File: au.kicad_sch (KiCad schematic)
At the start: 14 parts, among them Q1 SUM110P06-08L, Q2 2N7002, Q3 2N7002

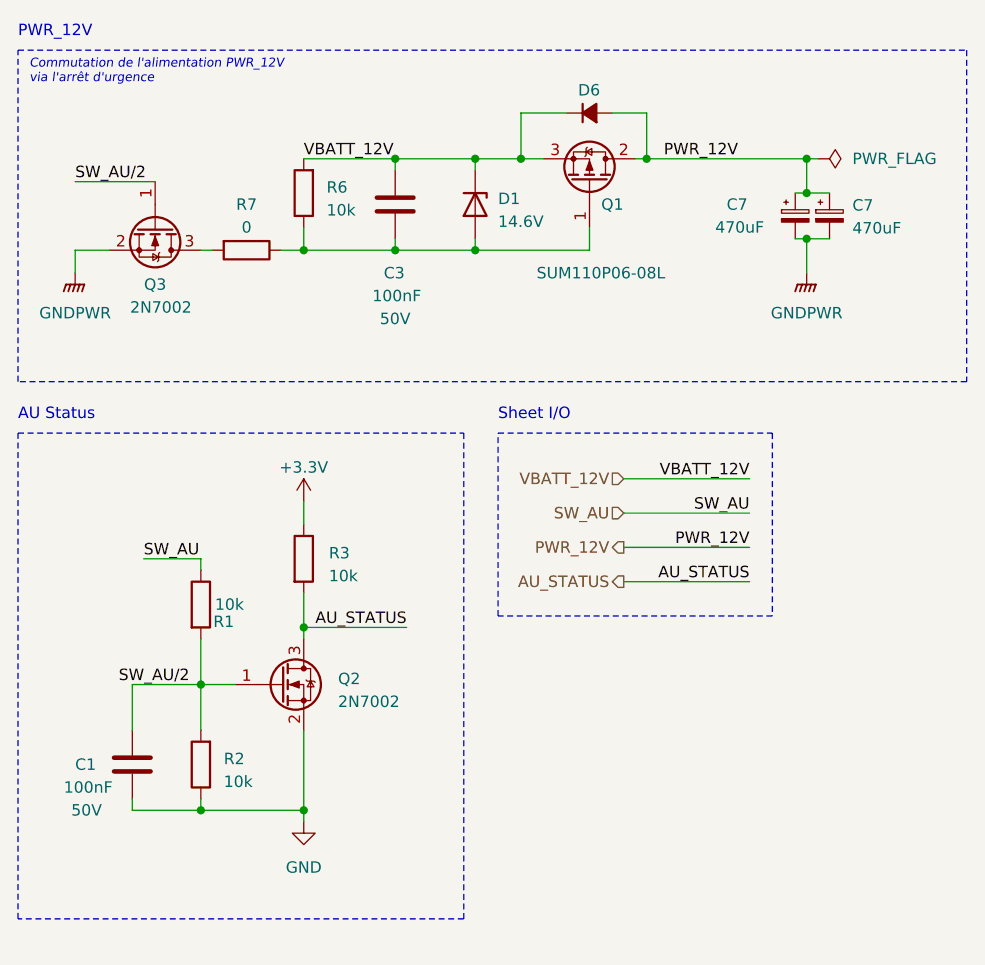
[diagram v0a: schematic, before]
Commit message: Correct CAN interface, add some filtering on sensors + add LCD board power connector
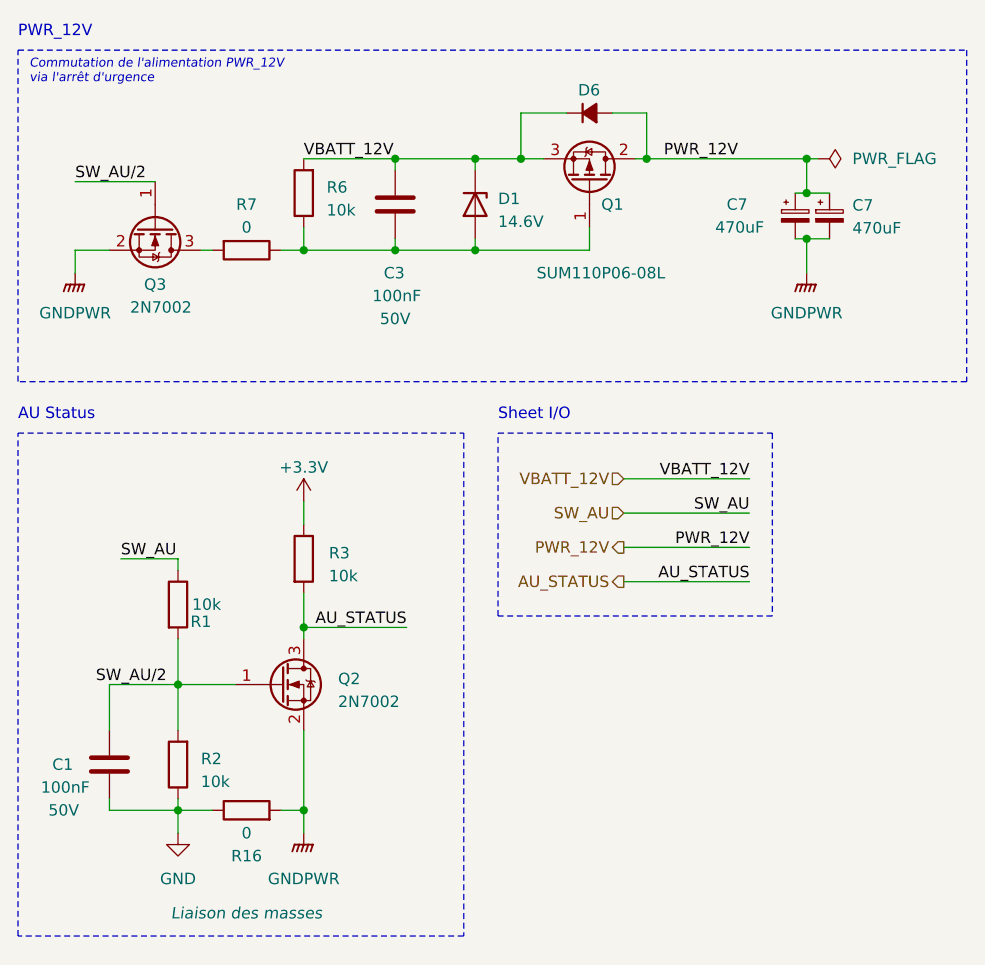
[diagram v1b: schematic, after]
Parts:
- added R16: 0, Resistor_SMD:R_0805_2012Metric, symbol Device:R
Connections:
- net GND: now also R16.1; no longer Q2.2 (S)
- net GNDPWR: now also Q2.2 (S), R16.2
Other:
- moved on the sheet: C1, R1, R2
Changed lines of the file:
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@@
   (junction (at 102.87 29.21) (diameter 0) (color 0 0 0 0)
   )
-  (junction (at 35.56 101.6) (diameter 0) (color 0 0 0 0)
+  (junction (at 33.02 101.6) (diameter 0) (color 0 0 0 0)
   )
-  (junction (at 35.56 87.63) (diameter 0) (color 0 0 0 0)
+  (junction (at 33.02 87.63) (diameter 0) (color 0 0 0 0)
   )
   (junction (at 102.87 33.02) (diameter 0) (color 0 0 0 0)
@@
     (stroke (width 0) (type default))
   )
-  (wire (pts (xy 35.56 82.55) (xy 35.56 87.63))
+  (wire (pts (xy 33.02 82.55) (xy 33.02 87.63))
     (stroke (width 0) (type default))
   )
@@
     (stroke (width 0) (type default))
   )
-  (wire (pts (xy 27.94 101.6) (xy 35.56 101.6))
+  (wire (pts (xy 25.4 101.6) (xy 33.02 101.6))
     (stroke (width 0) (type default))
   )
@@
     (stroke (width 0) (type default))
   )
-  (wire (pts (xy 35.56 87.63) (xy 39.37 87.63))
+  (wire (pts (xy 81.28 24.13) (xy 85.09 24.13))
     (stroke (width 0) (type default))
   )
-  (wire (pts (xy 81.28 24.13) (xy 85.09 24.13))
+  (wire (pts (xy 25.4 87.63) (xy 25.4 92.71))
     (stroke (width 0) (type default))
   )
-  (wire (pts (xy 27.94 87.63) (xy 27.94 92.71))
+  (wire (pts (xy 46.99 101.6) (xy 46.99 104.14))
     (stroke (width 0) (type default))
   )
-  (wire (pts (xy 46.99 101.6) (xy 46.99 102.87))
+  (wire (pts (xy 46.99 92.71) (xy 46.99 101.6))
     (stroke (width 0) (type default))
   )
@@
     (stroke (width 0) (type default))
   )
+  (wire (pts (xy 33.02 101.6) (xy 36.83 101.6))
+    (stroke (width 0) (type default))
+  )
   (wire (pts (xy 101.6 38.1) (xy 102.87 38.1))
     (stroke (width 0) (type default))
   )
+  (wire (pts (xy 33.02 101.6) (xy 33.02 104.14))
+    (stroke (width 0) (type default))
+  )
   (wire (pts (xy 66.04 39.37) (xy 57.15 39.37))
     (stroke (width 0) (type default))
@@
     (stroke (width 0) (type default))
   )
-  (wire (pts (xy 35.56 100.33) (xy 35.56 101.6))
+  (wire (pts (xy 33.02 100.33) (xy 33.02 101.6))
     (stroke (width 0) (type default))
   )
-  (wire (pts (xy 35.56 87.63) (xy 35.56 92.71))
+  (wire (pts (xy 33.02 87.63) (xy 33.02 92.71))
     (stroke (width 0) (type default))
   )
-  (wire (pts (xy 102.87 29.21) (xy 102.87 33.02))
+  (wire (pts (xy 33.02 87.63) (xy 39.37 87.63))
     (stroke (width 0) (type default))
   )
-  (wire (pts (xy 35.56 101.6) (xy 46.99 101.6))
+  (wire (pts (xy 102.87 29.21) (xy 102.87 33.02))
     (stroke (width 0) (type default))
   )
@@
     (stroke (width 0) (type default))
   )
-  (wire (pts (xy 27.94 100.33) (xy 27.94 101.6))
+  (wire (pts (xy 25.4 100.33) (xy 25.4 101.6))
     (stroke (width 0) (type default))
   )
@@
     (stroke (width 0) (type default))
   )
-  (wire (pts (xy 35.56 73.66) (xy 35.56 74.93))
+  (wire (pts (xy 33.02 73.66) (xy 33.02 74.93))
     (stroke (width 0) (type default))
   )
@@
     (stroke (width 0) (type default))
   )
-  (wire (pts (xy 46.99 92.71) (xy 46.99 101.6))
+  (wire (pts (xy 25.4 39.37) (xy 21.59 39.37))
     (stroke (width 0) (type default))
   )
-  (wire (pts (xy 25.4 39.37) (xy 21.59 39.37))
+  (wire (pts (xy 44.45 101.6) (xy 46.99 101.6))
     (stroke (width 0) (type default))
   )
@@
     (stroke (width 0) (type default))
   )
-  (wire (pts (xy 27.94 87.63) (xy 35.56 87.63))
+  (wire (pts (xy 25.4 87.63) (xy 33.02 87.63))
     (stroke (width 0) (type default))
   )
-  (wire (pts (xy 29.21 73.66) (xy 35.56 73.66))
+  (wire (pts (xy 26.67 73.66) (xy 33.02 73.66))
     (stroke (width 0) (type default))
   )
@@
     (fill (type none))
   )
-  (rectangle (start 15.24 59.69) (end 64.77 113.665)
+  (rectangle (start 15.24 59.69) (end 64.77 115.57)
     (stroke (width 0) (type dash))
     (fill (type none))
@@
     (effects (font (size 1.27 1.27)) (justify left bottom))
   )
-  (label "SW_AU{slash}2" (at 34.29 87.63 180) (fields_autoplaced)
+  (label "SW_AU{slash}2" (at 31.75 87.63 180) (fields_autoplaced)
     (effects (font (size 1.27 1.27)) (justify right bottom))
   )
@@
     (effects (font (size 1.27 1.27)) (justify right bottom))
   )
-  (label "SW_AU" (at 29.21 73.66 0) (fields_autoplaced)
+  (label "SW_AU" (at 26.67 73.66 0) (fields_autoplaced)
     (effects (font (size 1.27 1.27)) (justify left bottom))
   )
@@
     (effects (font (size 1.27 1.27)) (justify right))
   )
-  (symbol (lib_id "Device:R") (at 35.56 96.52 180) (unit 1)
+  (symbol (lib_id "Device:R") (at 33.02 96.52 180) (unit 1)
     (in_bom yes) (on_board yes) (dnp no) (fields_autoplaced)
-    (property "Reference" "R2" (at 38.1 95.885 0)
+    (property "Reference" "R2" (at 35.56 95.885 0)
       (effects (font (size 1.27 1.27)) (justify right))
     )
-    (property "Value" "10k" (at 38.1 98.425 0)
+    (property "Value" "10k" (at 35.56 98.425 0)
       (effects (font (size 1.27 1.27)) (justify right))
     )
-    (property "Footprint" "Resistor_SMD:R_0603_1608Metric" (at 37.338 96.52 90)
+    (property "Footprint" "Resistor_SMD:R_0603_1608Metric" (at 34.798 96.52 90)
       (effects (font (size 1.27 1.27)) hide)
     )
-    (property "Datasheet" "~" (at 35.56 96.52 0)
+    (property "Datasheet" "~" (at 33.02 96.52 0)
       (effects (font (size 1.27 1.27)) hide)
     )
@@
     )
   )
-  (symbol (lib_id "Device:C") (at 27.94 96.52 0) (unit 1)
+  (symbol (lib_id "Device:R") (at 40.64 101.6 90) (unit 1)
     (in_bom yes) (on_board yes) (dnp no)
-    (property "Reference" "C1" (at 21.59 96.52 0)
+    (property "Reference" "R16" (at 40.64 106.68 90)
+      (effects (font (size 1.27 1.27)))
+    )
+    (property "Value" "0" (at 40.64 104.14 90)
+      (effects (font (size 1.27 1.27)))
+    )
+    (property "Footprint" "Resistor_SMD:R_0805_2012Metric" (at 40.64 103.378 90)
+      (effects (font (size 1.27 1.27)) hide)
+    )
+    (property "Datasheet" "~" (at 40.64 101.6 0)
+      (effects (font (size 1.27 1.27)) hide)
+    )
+    (property "Description" "Liaison des masses" (at 40.64 113.03 90)
+      (effects (font (size 1.27 1.27) italic (color 0 132 132 1)))
+    )
+    (pin "1")
+    (pin "2")
+    (instances
+      (project "12v-actuators-pcb"
+        (path "/d0b6cc72-ff07-4f5e-a148-04b65c86a715"
+          (reference "R16") (unit 1)
+        )
+        (path "/d0b6cc72-ff07-4f5e-a148-04b65c86a715/a9998e65-7bac-4337-98c8-7de7c845405f"
+          (reference "R16") (unit 1)
+        )
+      )
+    )
+  )
+  (symbol (lib_id "Device:C") (at 25.4 96.52 0) (unit 1)
+    (in_bom yes) (on_board yes) (dnp no)
+    (property "Reference" "C1" (at 19.05 96.52 0)
       (effects (font (size 1.27 1.27)) (justify left))
     )
-    (property "Value" "100nF" (at 20.32 99.06 0)
+    (property "Value" "100nF" (at 17.78 99.06 0)
       (effects (font (size 1.27 1.27)) (justify left))
     )
-    (property "Footprint" "Capacitor_SMD:C_0603_1608Metric" (at 28.9052 100.33 0)
+    (property "Footprint" "Capacitor_SMD:C_0603_1608Metric" (at 26.3652 100.33 0)
       (effects (font (size 1.27 1.27)) hide)
     )
-    (property "Datasheet" "~" (at 27.94 96.52 0)
+    (property "Datasheet" "~" (at 25.4 96.52 0)
       (effects (font (size 1.27 1.27)) hide)
     )
-    (property "Max voltage" "50V" (at 22.86 101.6 0)
+    (property "Max voltage" "50V" (at 20.32 101.6 0)
       (effects (font (size 1.27 1.27) (color 0 132 132 1)))
     )
@@
     )
   )
-  (symbol (lib_id "Device:R") (at 35.56 78.74 0) (unit 1)
+  (symbol (lib_id "Device:R") (at 33.02 78.74 0) (unit 1)
     (in_bom yes) (on_board yes) (dnp no)
-    (property "Reference" "R1" (at 38.1 80.645 0)
+    (property "Reference" "R1" (at 35.56 80.645 0)
       (effects (font (size 1.27 1.27)))
     )
-    (property "Value" "10k" (at 38.735 78.74 0)
+    (property "Value" "10k" (at 36.195 78.74 0)
       (effects (font (size 1.27 1.27)))
     )
-    (property "Footprint" "Resistor_SMD:R_0201_0603Metric" (at 33.782 78.74 90)
+    (property "Footprint" "Resistor_SMD:R_0201_0603Metric" (at 31.242 78.74 90)
       (effects (font (size 1.27 1.27)) hide)
     )
-    (property "Datasheet" "~" (at 35.56 78.74 0)
+    (property "Datasheet" "~" (at 33.02 78.74 0)
       (effects (font (size 1.27 1.27)) hide)
     )
@@
     )
   )
+  (symbol (lib_id "power:GNDPWR") (at 46.99 104.14 0) (unit 1)
+    (in_bom yes) (on_board yes) (dnp no)
+    (property "Reference" "#PWR030" (at 46.99 109.22 0)
+      (effects (font (size 1.27 1.27)) hide)
+    )
+    (property "Value" "GNDPWR" (at 46.99 109.22 0)
+      (effects (font (size 1.27 1.27)))
+    )
+    (property "Footprint" "" (at 46.99 105.41 0)
+      (effects (font (size 1.27 1.27)) hide)
+    )
+    (property "Datasheet" "" (at 46.99 105.41 0)
+      (effects (font (size 1.27 1.27)) hide)
+    )
+    (pin "1")
+    (instances
+      (project "12v-actuators-pcb"
+        (path "/d0b6cc72-ff07-4f5e-a148-04b65c86a715"
+          (reference "#PWR030") (unit 1)
+        )
+        (path "/d0b6cc72-ff07-4f5e-a148-04b65c86a715/a9998e65-7bac-4337-98c8-7de7c845405f"
+          (reference "#PWR041") (unit 1)
+        )
+      )
+    )
+  )
   (symbol (lib_id "power:GNDPWR") (at 102.87 41.91 0) (unit 1)
     (in_bom yes) (on_board yes) (dnp no)
@@
     )
   )
-  (symbol (lib_id "power:GND") (at 46.99 102.87 0) (unit 1)
+  (symbol (lib_id "power:GND") (at 33.02 104.14 0) (unit 1)
     (in_bom yes) (on_board yes) (dnp no) (fields_autoplaced)
-    (property "Reference" "#PWR05" (at 46.99 109.22 0)
+    (property "Reference" "#PWR05" (at 33.02 110.49 0)
       (effects (font (size 1.27 1.27)) hide)
     )
-    (property "Value" "GND" (at 46.99 107.95 0)
+    (property "Value" "GND" (at 33.02 109.22 0)
       (effects (font (size 1.27 1.27)))
     )
-    (property "Footprint" "" (at 46.99 102.87 0)
+    (property "Footprint" "" (at 33.02 104.14 0)
       (effects (font (size 1.27 1.27)) hide)
     )
-    (property "Datasheet" "" (at 46.99 102.87 0)
+    (property "Datasheet" "" (at 33.02 104.14 0)
       (effects (font (size 1.27 1.27)) hide)
     )

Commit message: Few details -> add filtering on 35A ESC signals + 3.3V capa ...
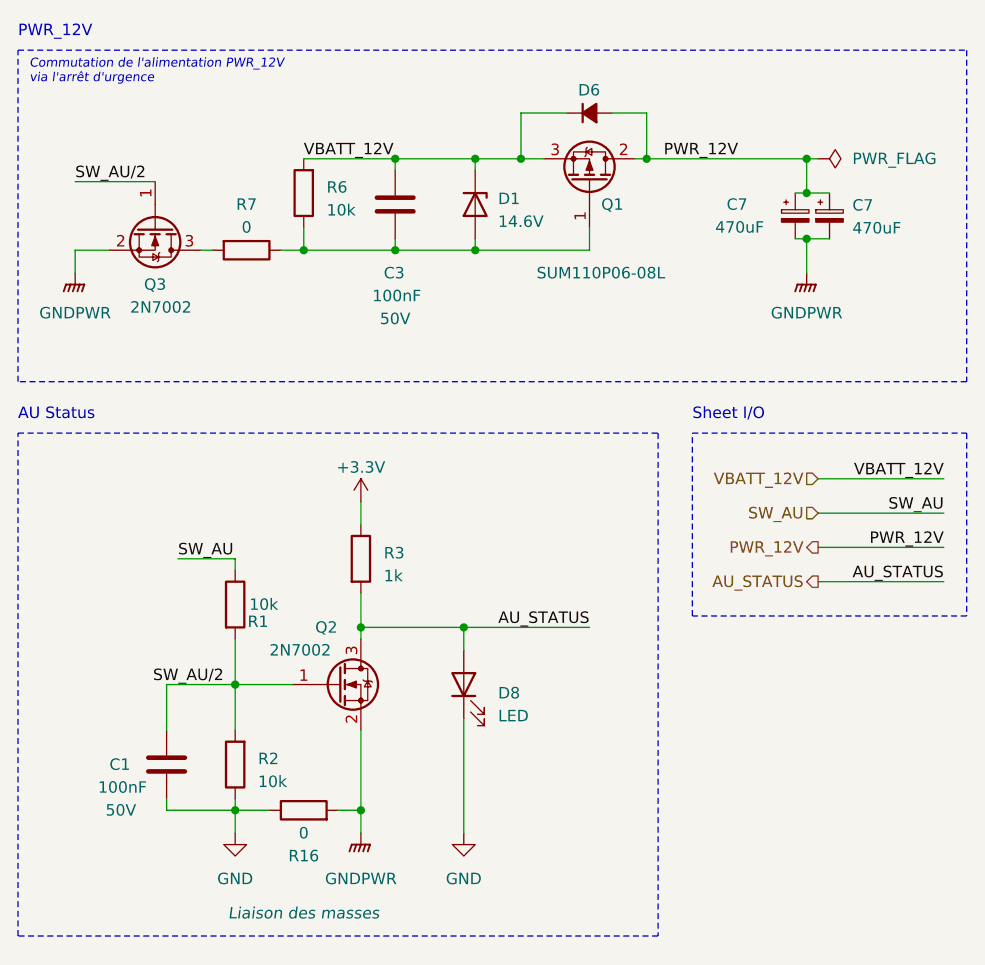
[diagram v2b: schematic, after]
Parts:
- added D8: LED, LED_SMD:LED_0603_1608Metric, symbol Device:LED
- R3: value 10k -> 1k
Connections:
- net AU_STATUS: now also D8.2 (A)
- net GND: now also D8.1 (K)
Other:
- moved on the sheet: C1, Q2, R1, R16, R2, R3

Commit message: Schematics finished, reanotated sch
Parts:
- added R2: 10k, Resistor_SMD:R_0603_1608Metric, symbol Device:R
- R1: value 10k -> 4.7k; footprint Resistor_SMD:R_0201_0603Metric -> Resistor_SMD:R_0603_1608Metric
- R3: value 1k -> 10k
- R6, R7: footprint Resistor_SMD:R_0201_0603Metric -> Resistor_SMD:R_0603_1608Metric
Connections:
- net AU_STATUS: no longer D8.2 (A)
- net GND: now also R2.2; no longer D8.1 (K)
- net SW_AU/2: now also D8.2 (A)
- new net: D8.1 (K), R2.1
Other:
- moved on the sheet: C1, D8, Q2, R1, R16, R2, R3

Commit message: Update schematic pinout for LED_EN + Add mechanical constraints to PCB layout
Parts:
- Q1: footprint Package_TO_SOT_SMD:TO-252-2 -> Package_TO_SOT_SMD:TO-263-2
- R16: footprint Resistor_SMD:R_0805_2012Metric -> Capacitor_SMD:C_0603_1608Metric
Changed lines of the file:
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@@
       (effects (font (size 1.27 1.27)))
     )
-    (property "Footprint" "Resistor_SMD:R_0805_2012Metric" (at 59.69 103.378 90)
+    (property "Footprint" "Capacitor_SMD:C_0603_1608Metric" (at 59.69 103.378 90)
       (effects (font (size 1.27 1.27)) hide)
     )
@@
       (effects (font (size 1.27 1.27)))
     )
-    (property "Footprint" "Package_TO_SOT_SMD:TO-252-2" (at 76.835 26.67 0)
+    (property "Footprint" "Package_TO_SOT_SMD:TO-263-2" (at 76.835 26.67 0)
       (effects (font (size 1.27 1.27) italic) (justify left) hide)
     )
-    (property "Datasheet" "http://www.jaolen.com/images/pdf/QM6015D.pdf" (at 78.74 31.75 90)
+    (property "Datasheet" "https://www.vishay.com/docs/73045/73045.pdf" (at 78.74 31.75 90)
       (effects (font (size 1.27 1.27)) (justify left) hide)
     )
